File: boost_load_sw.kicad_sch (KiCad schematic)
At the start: 0 parts

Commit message: Working on power board
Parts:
- added U5: PTPS16850VMAR, VMA0023A-MFG, symbol _TPS1685:PTPS16850VMAR
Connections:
- new net BOOST_IN: U5.10 (IN), U5.22 (IN), U5.23 (IN), U5.24 (IN)
- new net VBUS: U5.7 (OUT), U5.8 (OUT)
- no-connect marks 0 -> 3

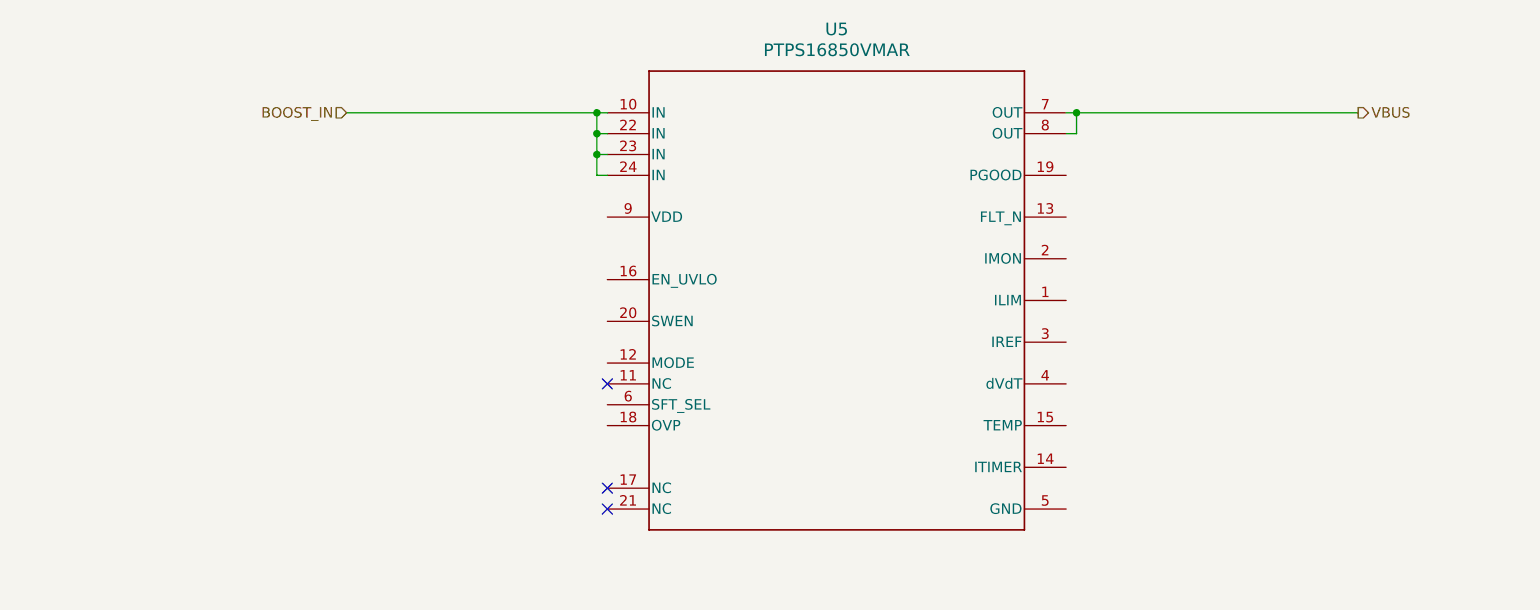
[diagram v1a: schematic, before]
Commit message: Adding more schematic blocks
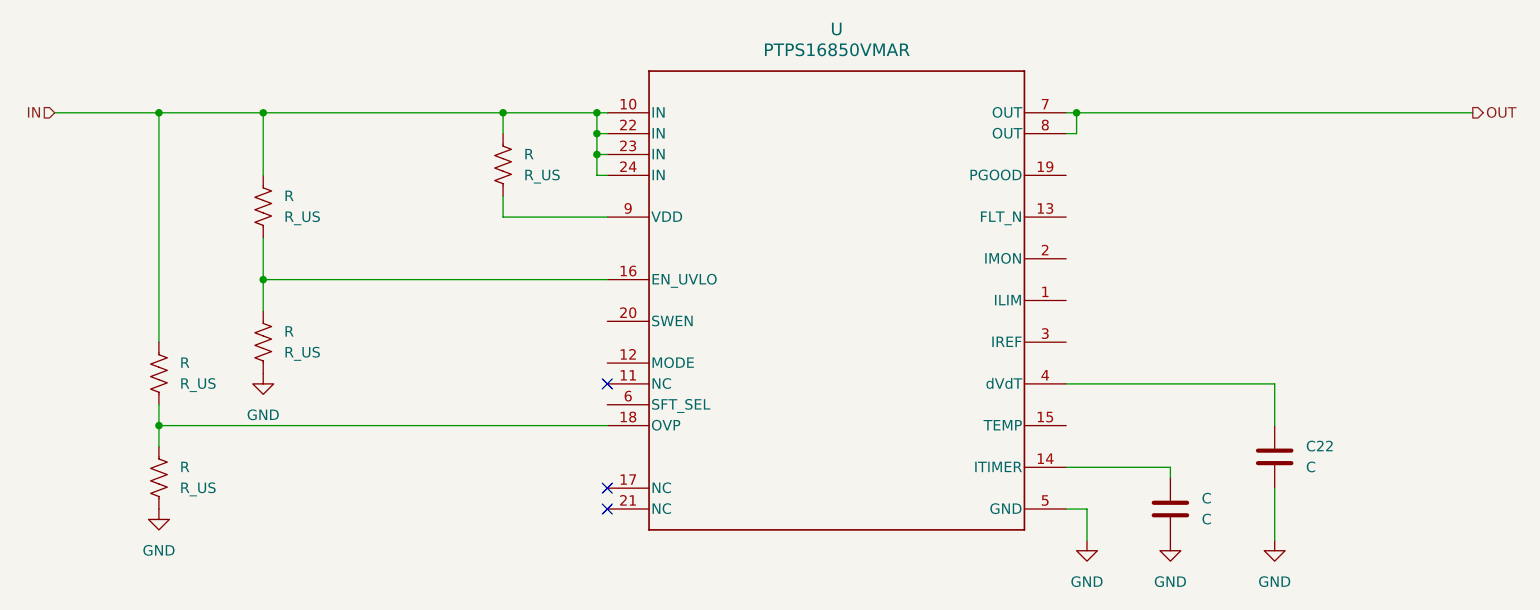
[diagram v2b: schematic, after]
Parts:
- added C, C22: C, symbol Device:C
- added R (x5): R_US, symbol Device:R_US
- renumbered U5 to U
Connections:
- net at U.14 (ITIMER): now also C.1
- net at U.16 (EN_UVLO): now also R.1, R.2
- net at U.18 (OVP): now also R.1, R.2
- net at U.4 (dVdT): now also C22.1
- net GND: now reaches U.5 (GND)
- net GND: now also C.2, C22.2, R.2, R.2
- net at U.9 (VDD): now also R.2
- net BOOST_IN renamed IN
- net IN: now also R.1, R.1, R.1
- net VBUS renamed OUT

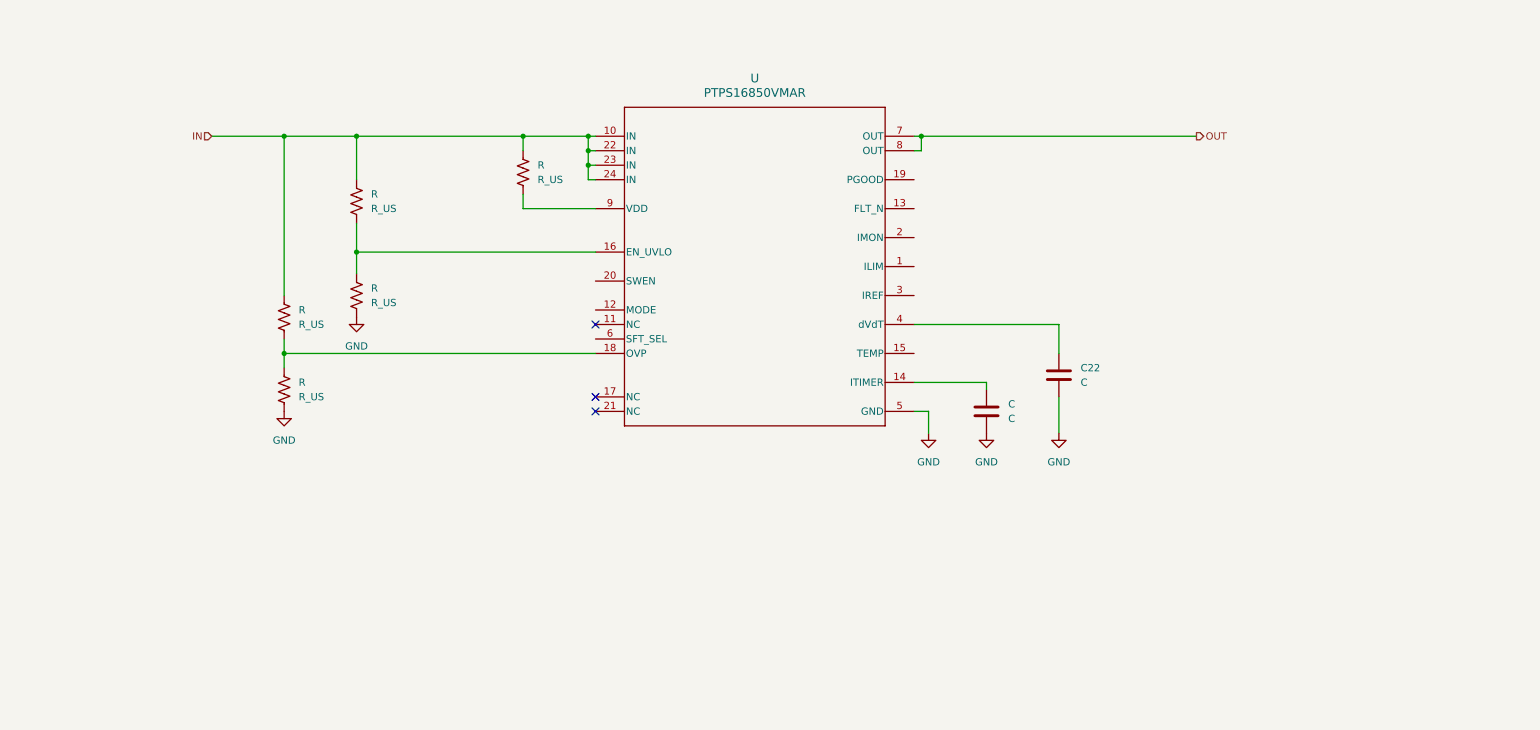
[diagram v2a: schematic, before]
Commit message: Working on load switches
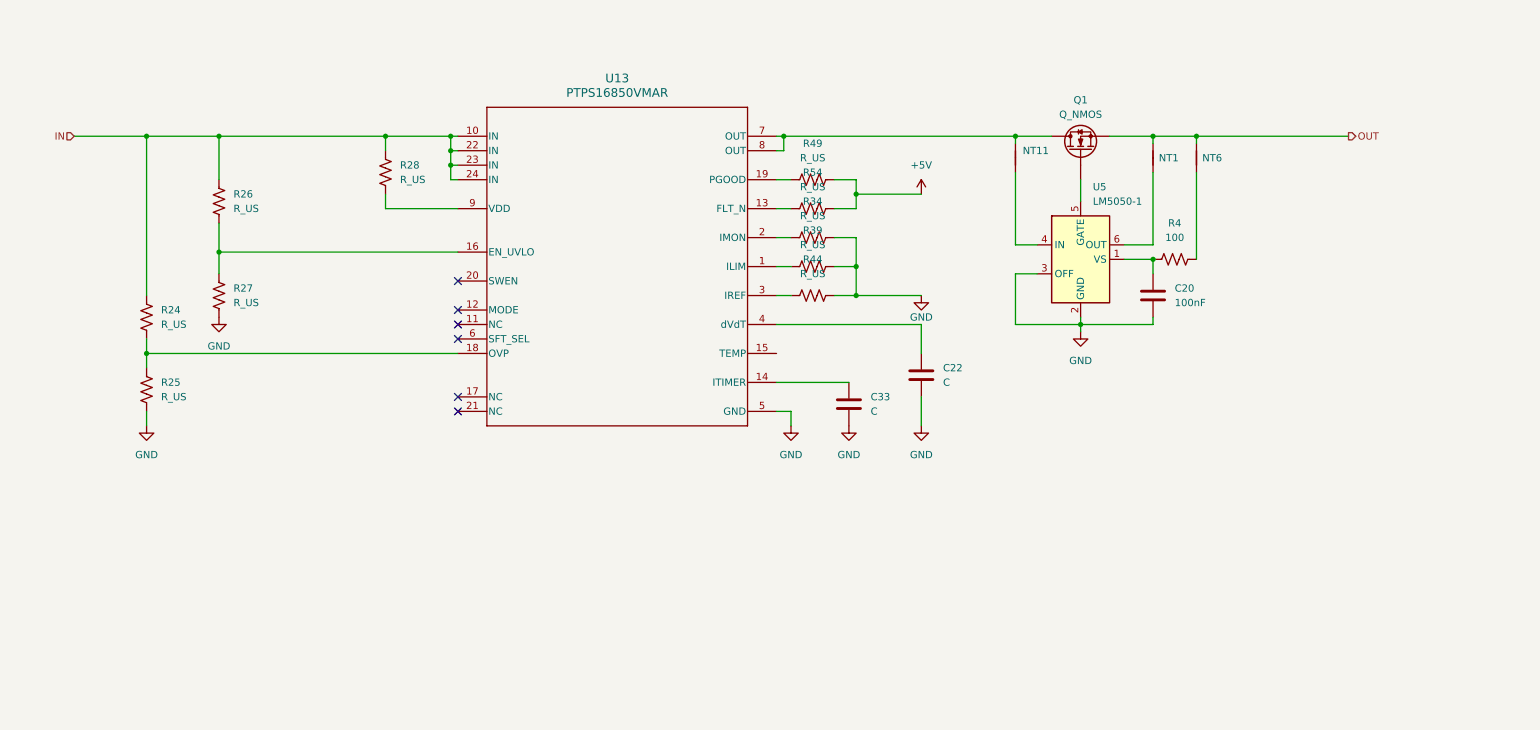
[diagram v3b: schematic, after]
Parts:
- added C20: 100nF, symbol Device:C
- added NT1, NT11, NT6: NetTie_2, symbol Device:NetTie_2
- added Q1: Q_NMOS, symbol Device:Q_NMOS
- added R34, R39, R44, R49, R54: R_US, symbol Device:R_US
- added R4: 100, symbol Device:R_US
- added U5: LM5050-1, Package_TO_SOT_SMD:TSOT-23-6, symbol Power_Management:LM5050-1
- renumbered C to C33, R to R24, R to R25, R to R26, R to R27, R to R28, U to U13
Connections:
- net GND: now also C20.2, R34.2, R39.2, R44.2, U5.2 (GND), U5.3 (OFF)
- net OUT: now also NT1.2, NT6.2, Q1.S; no longer U13.7 (OUT), U13.8 (OUT)
- net at U13.1 (ILIM): now also R39.1
- net at U13.13 (FLT_N): now also R54.1
- net at U13.19 (PGOOD): now also R49.1
- net at U13.2 (IMON): now also R34.1
- net at U13.3 (IREF): now also R44.1
- new net: NT11.1, U5.4 (IN)
- new net: NT11.2, Q1.D, U13.7 (OUT), U13.8 (OUT)
- new net: C20.1, R4.1, U5.1 (VS)
- new net: NT6.1, R4.2
- new net: Q1.G, U5.5 (GATE)
- new net: NT1.1, U5.6 (OUT)
- new net +5V: R49.2, R54.2
- no-connect marks 3 -> 6
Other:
- moved on the sheet: C22, C33, R24, R25, R26, R27, R28, U13

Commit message: Working on load switch design
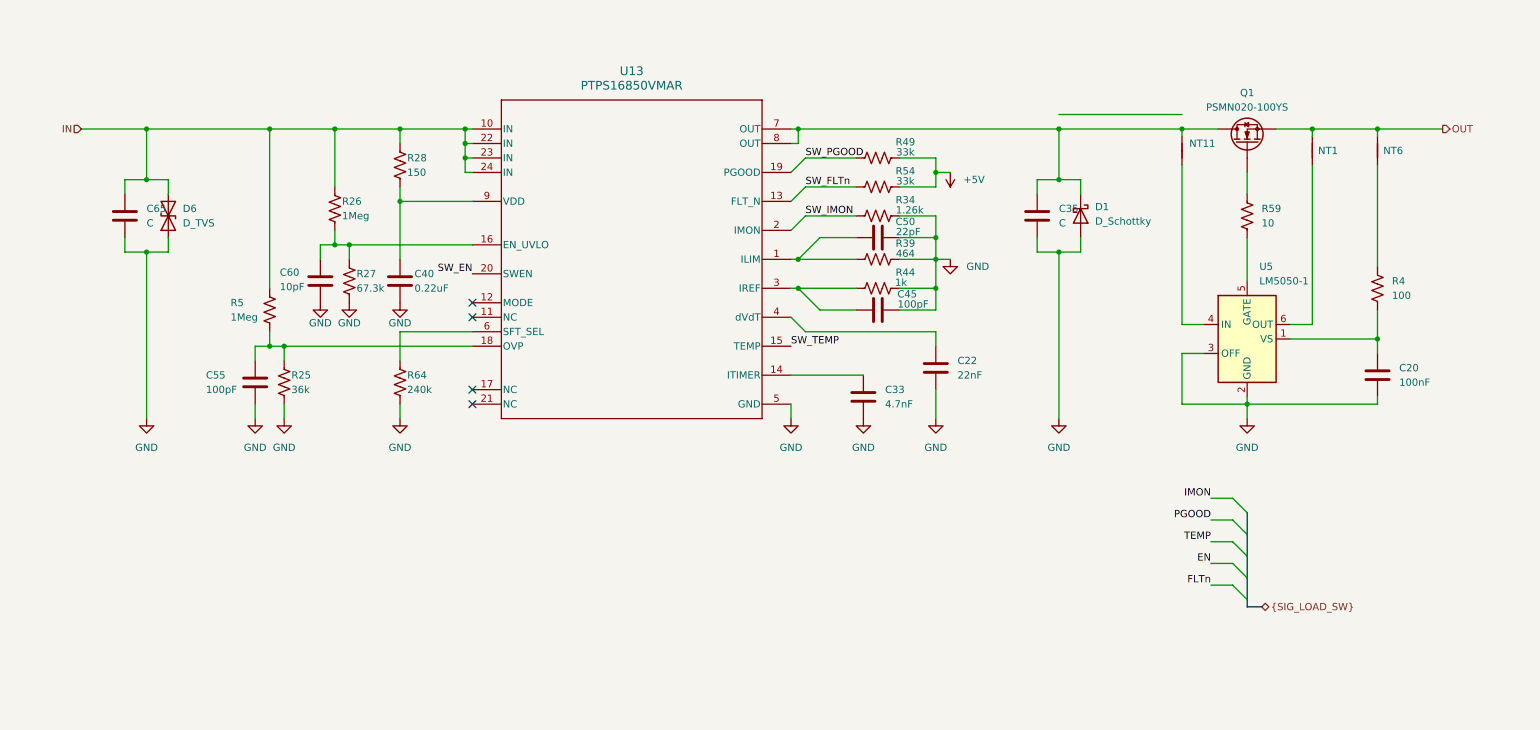
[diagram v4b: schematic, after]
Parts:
- removed R24: R_US, symbol Device:R_US
- added C35, C65: C, symbol Device:C
- added C40: 0.22uF, Capacitor_SMD:C_0603_1608Metric, symbol Device:C
- added C45, C55: 100pF, Capacitor_SMD:C_0603_1608Metric, symbol Device:C
- added C50: 22pF, Capacitor_SMD:C_0603_1608Metric, symbol Device:C
- added C60: 10pF, Capacitor_SMD:C_0603_1608Metric, symbol Device:C
- added D1: D_Schottky, symbol Device:D_Schottky
- added D6: D_TVS, symbol Device:D_TVS
- added R5: 1Meg, Resistor_SMD:R_0603_1608Metric, symbol Device:R_US
- added R59: 10, Resistor_SMD:R_1206_3216Metric, symbol Device:R_US
- added R64: 240k, Resistor_SMD:R_0603_1608Metric, symbol Device:R_US
- C20: footprint (none) -> Capacitor_SMD:C_0805_2012Metric; Mfr (none) -> KYOCERA AVX; Mfr P/N (none) -> 08055C104J4T2A; Supplier_1 (none) -> Digikey; Supplier_1 P/N (none) -> 478-KAM21BR71H104JTTR-ND; Supplier_1 Price @ Qty (none) -> 1; Supplier_1 Unit Price (none) -> 0.18000
- C22: value C -> 22nF; footprint (none) -> Capacitor_SMD:C_0805_2012Metric; Mfr (none) -> Murata Electronics; Mfr P/N (none) -> GCM21B5C1H223FA16L; Supplier_1 (none) -> Digikey; Supplier_1 P/N (none) -> 490-GCM21B5C1H223FA16LTR-ND; Supplier_1 Price @ Qty (none) -> 1; Supplier_1 Unit Price (none) -> 0.52000
- C33: value C -> 4.7nF; footprint (none) -> Resistor_SMD:R_0603_1608Metric; Mfr (none) -> Murata Electronics; Mfr P/N (none) -> GCM1885C2A471FA16D; Supplier_1 (none) -> Digikey; Supplier_1 P/N (none) -> 490-GCM1885C2A471FA16DTR-ND; Supplier_1 Price @ Qty (none) -> 1; Supplier_1 Unit Price (none) -> 0.16000
- Q1: value Q_NMOS -> PSMN020-100YS; footprint (none) -> Package_TO_SOT_SMD:LFPAK56; Mfr (none) -> Nexperia USA Inc.; Mfr P/N (none) -> PSMN020-100YS,115; Supplier_1 (none) -> Digikey; Supplier_1 P/N (none) -> 1727-4286-2-ND; Supplier_1 Price @ Qty (none) -> 1; Supplier_1 Unit Price (none) -> 1.42000
- R25: value R_US -> 36k; footprint (none) -> Resistor_SMD:R_0603_1608Metric; Mfr (none) -> Panasonic Electronic Components; Mfr P/N (none) -> ERA-3AEB363V; Supplier_1 (none) -> Digikey; Supplier_1 P/N (none) -> P36KDBTR-ND; Supplier_1 Price @ Qty (none) -> 1; Supplier_1 Unit Price (none) -> 0.10000
- R26: value R_US -> 1Meg; footprint (none) -> Resistor_SMD:R_0603_1608Metric; Mfr (none) -> Stackpole Electronics Inc; Mfr P/N (none) -> RNCF0603BKC1M00; Supplier_1 (none) -> Digikey; Supplier_1 P/N (none) -> RNCF0603BKC1M00TR-ND; Supplier_1 Price @ Qty (none) -> 1; Supplier_1 Unit Price (none) -> 0.11000
- R27: value R_US -> 67.3k; footprint (none) -> Resistor_SMD:R_0603_1608Metric; Mfr (none) -> KOA Speer Electronics, Inc.; Mfr P/N (none) -> RN73R1JTTD6732B25; Supplier_1 (none) -> Digikey; Supplier_1 P/N (none) -> 2019-RN73R1JTTD6732B25TR-ND; Supplier_1 Price @ Qty (none) -> 1; Supplier_1 Unit Price (none) -> 0.12000
- R28: value R_US -> 150; footprint (none) -> Resistor_SMD:R_0603_1608Metric; Mfr (none) -> Panasonic Electronic Components; Mfr P/N (none) -> ERA-3AEB151V; Supplier_1 (none) -> Digikey; Supplier_1 P/N (none) -> P150DBTR-ND; Supplier_1 Price @ Qty (none) -> 1; Supplier_1 Unit Price (none) -> 0.10000
- R34: value R_US -> 1.26k; footprint (none) -> Resistor_SMD:R_0603_1608Metric; Mfr (none) -> KOA Speer Electronics, Inc.; Mfr P/N (none) -> RN73R1JTTD1261B25; Supplier_1 (none) -> Digikey; Supplier_1 P/N (none) -> 2019-RN73R1JTTD1261B25TR-ND; Supplier_1 Price @ Qty (none) -> 1; Supplier_1 Unit Price (none) -> 0.12000
- R39: value R_US -> 464; footprint (none) -> Resistor_SMD:R_0603_1608Metric; Mfr (none) -> Panasonic Electronic Components; Mfr P/N (none) -> ERA-3AEB4640V; Supplier_1 (none) -> Digikey; Supplier_1 P/N (none) -> 10-ERA-3AEB4640VTR-ND; Supplier_1 Price @ Qty (none) -> 1; Supplier_1 Unit Price (none) -> 0.10000
- R4: footprint (none) -> Resistor_SMD:R_0603_1608Metric; Mfr (none) -> Panasonic Electronic Components; Mfr P/N (none) -> ERA-3AEB101V; Supplier_1 (none) -> Digikey; Supplier_1 P/N (none) -> P100DBTR-ND; Supplier_1 Price @ Qty (none) -> 1; Supplier_1 Unit Price (none) -> 0.10000
- R44: value R_US -> 1k; footprint (none) -> Resistor_SMD:R_0603_1608Metric; Mfr (none) -> Panasonic Electronic Components; Mfr P/N (none) -> ERA-3AEB103V; Supplier_1 (none) -> Digikey; Supplier_1 P/N (none) -> P10KDBTR-ND; Supplier_1 Price @ Qty (none) -> 1; Supplier_1 Unit Price (none) -> 0.10000
- R49, R54: value R_US -> 33k; footprint (none) -> Resistor_SMD:R_0603_1608Metric; Mfr (none) -> Panasonic Electronic Components; Mfr P/N (none) -> ERA-3AEB333V; Supplier_1 (none) -> Digikey; Supplier_1 P/N (none) -> P33KDBTR-ND; Supplier_1 Price @ Qty (none) -> 1; Supplier_1 Unit Price (none) -> 0.10000
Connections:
- net GND: now also C35.2, C40.2, C45.2, C50.2, C55.2, C60.2, C65.2, D1.2 (A), D6.1 (A1), R64.2
- net IN: now also C65.1, D6.2 (A2), R5.1
- net at NT11.2, Q1.D, U13.7 (OUT)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: now also C35.1, D1.1 (K)
- net at R39.1, U13.1 (ILIM): now also C50.1
- net SW_PGOOD: now reaches R49.1, U13.19 (PGOOD)
- net at R26.2, R27.1, U13.16 (EN_UVLO): now also C60.1
- net SW_FLTn: now reaches R54.1, U13.13 (FLT_N)
- net SW_IMON: now reaches R34.1, U13.2 (IMON)
- net SW_TEMP: now reaches U13.15 (TEMP)
- net at R25.1, U13.18 (OVP): now also C55.1, R5.2
- net SW_EN: now reaches U13.20 (SWEN)
- net at R44.1, U13.3 (IREF): now also C45.1
- net at U13.6 (SFT_SEL): now also R64.1
- net at R28.2, U13.9 (VDD): now also C40.1
- net at Q1.G: now also R59.1; no longer U5.5 (GATE)
- new net: R59.2, U5.5 (GATE)
- no-connect marks 6 -> 4
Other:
- company: (none) -> Solar Airplane
- title: (none) -> Load Switch
- moved on the sheet: C20, C22, C33, NT1, NT11, NT6, Q1, R25, R26, R27, R28, R34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

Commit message: Adding surge protection and comments to lsw
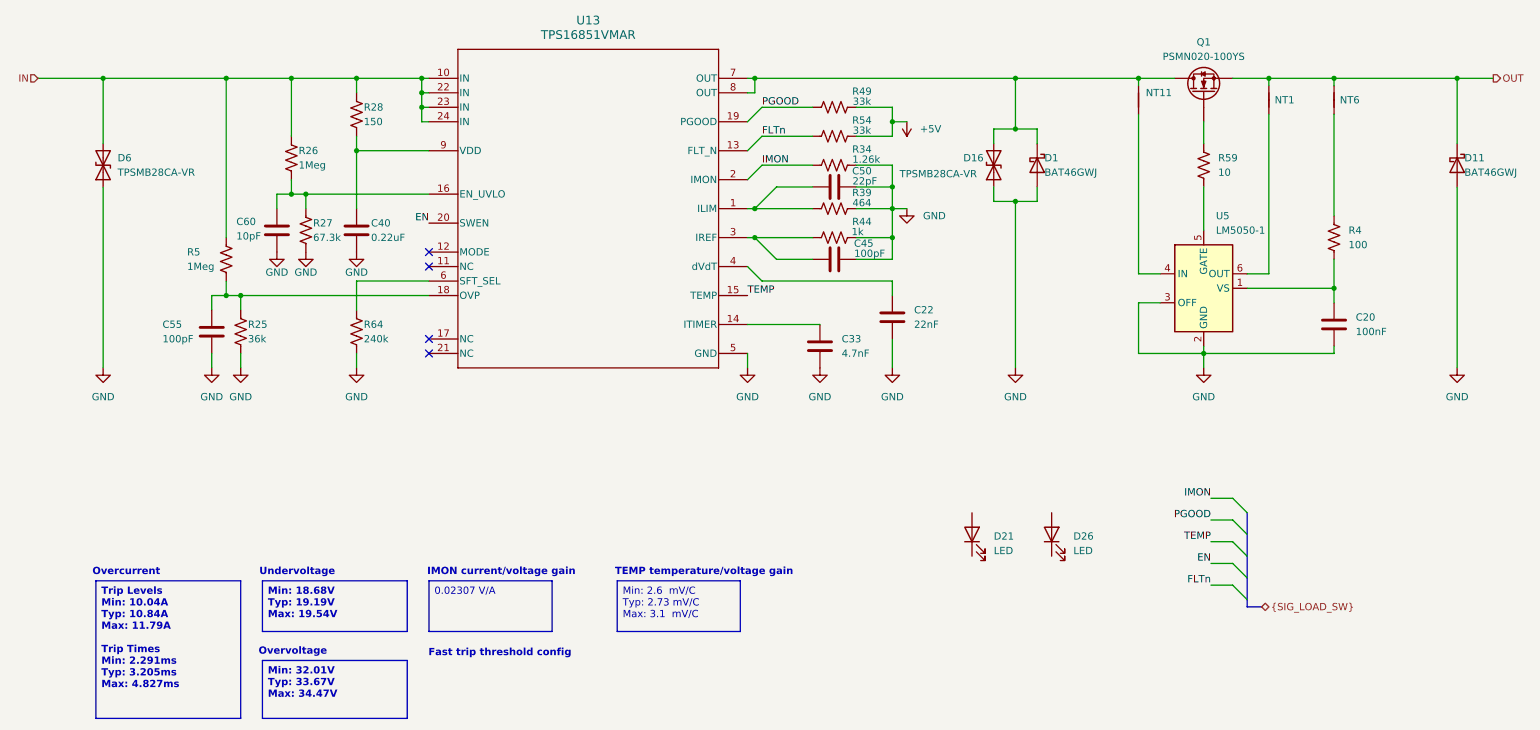
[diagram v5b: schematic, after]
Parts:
- removed C35, C65: C, symbol Device:C
- added D11: BAT46GWJ, Diode_SMD:D_SOD-123, symbol Device:D_Schottky
- added D16: TPSMB28CA-VR, Diode_SMD:D_SMB, symbol Device:D_TVS
- added D21, D26: LED, symbol Device:LED
- D1: value D_Schottky -> BAT46GWJ; footprint (none) -> Diode_SMD:D_SOD-123; Mfr (none) -> Nexperia USA Inc.; Mfr P/N (none) -> BAT46GWJ; Supplier_1 (none) -> Digikey; Supplier_1 P/N (none) -> 1727-7326-2-ND; Supplier_1 Price @ Qty (none) -> 0.19000; Supplier_1 Unit Price (none) -> 1
- D6: value D_TVS -> TPSMB28CA-VR; footprint (none) -> Diode_SMD:D_SMB; Mfr (none) -> Littelfuse Inc.; Mfr P/N (none) -> TPSMB28CA-VR; Supplier_1 (none) -> Digikey; Supplier_1 P/N (none) -> TPSMB28CA-VRTR-ND; Supplier_1 Price @ Qty (none) -> 1; Supplier_1 Unit Price (none) -> 0.23000
- U13: value PTPS16850VMAR -> TPS16851VMAR; Mfr (none) -> Texas Instruments; Mfr P/N (none) -> TPS16851VMAR; Supplier_1 (none) -> Texas Instruments; Supplier_1 P/N (none) -> TPS16851VMAR; Supplier_1 Price @ Qty (none) -> 1; Supplier_1 Unit Price (none) -> 10.32
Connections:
- net SW_EN is gone; now on net EN: U13.20 (SWEN)
- net SW_FLTn is gone; now on net FLTn: R54.1, U13.13 (FLT_N)
- net SW_IMON is gone; now on net IMON: R34.1, U13.2 (IMON)
- net SW_PGOOD is gone; now on net PGOOD: R49.1, U13.19 (PGOOD)
- net SW_TEMP is gone; now on net TEMP: U13.15 (TEMP)
- net GND: now also D11.2 (A), D16.1 (A1)
- net OUT: now also D11.1 (K)
- net at D1.1 (K), NT11.2, Q1.D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: now also D16.2 (A2)
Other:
- note added: "Fast trip threshold config"
- note added: "IMON current/voltage gain"
- note added: "Overcurrent"
- note added: "Overvoltage"
- note added: "TEMP temperature/voltage gain"
- note added: "Undervoltage"
- moved on the sheet: C20, C22, C33, C40, C45, C50, C55, C60, D1, D6, NT1, NT11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
